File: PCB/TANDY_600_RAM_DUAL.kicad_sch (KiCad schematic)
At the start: 5 parts, among them J1 DIN 41612 2x22 male right-ang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, U1 628128_SOP, U2 74HC08

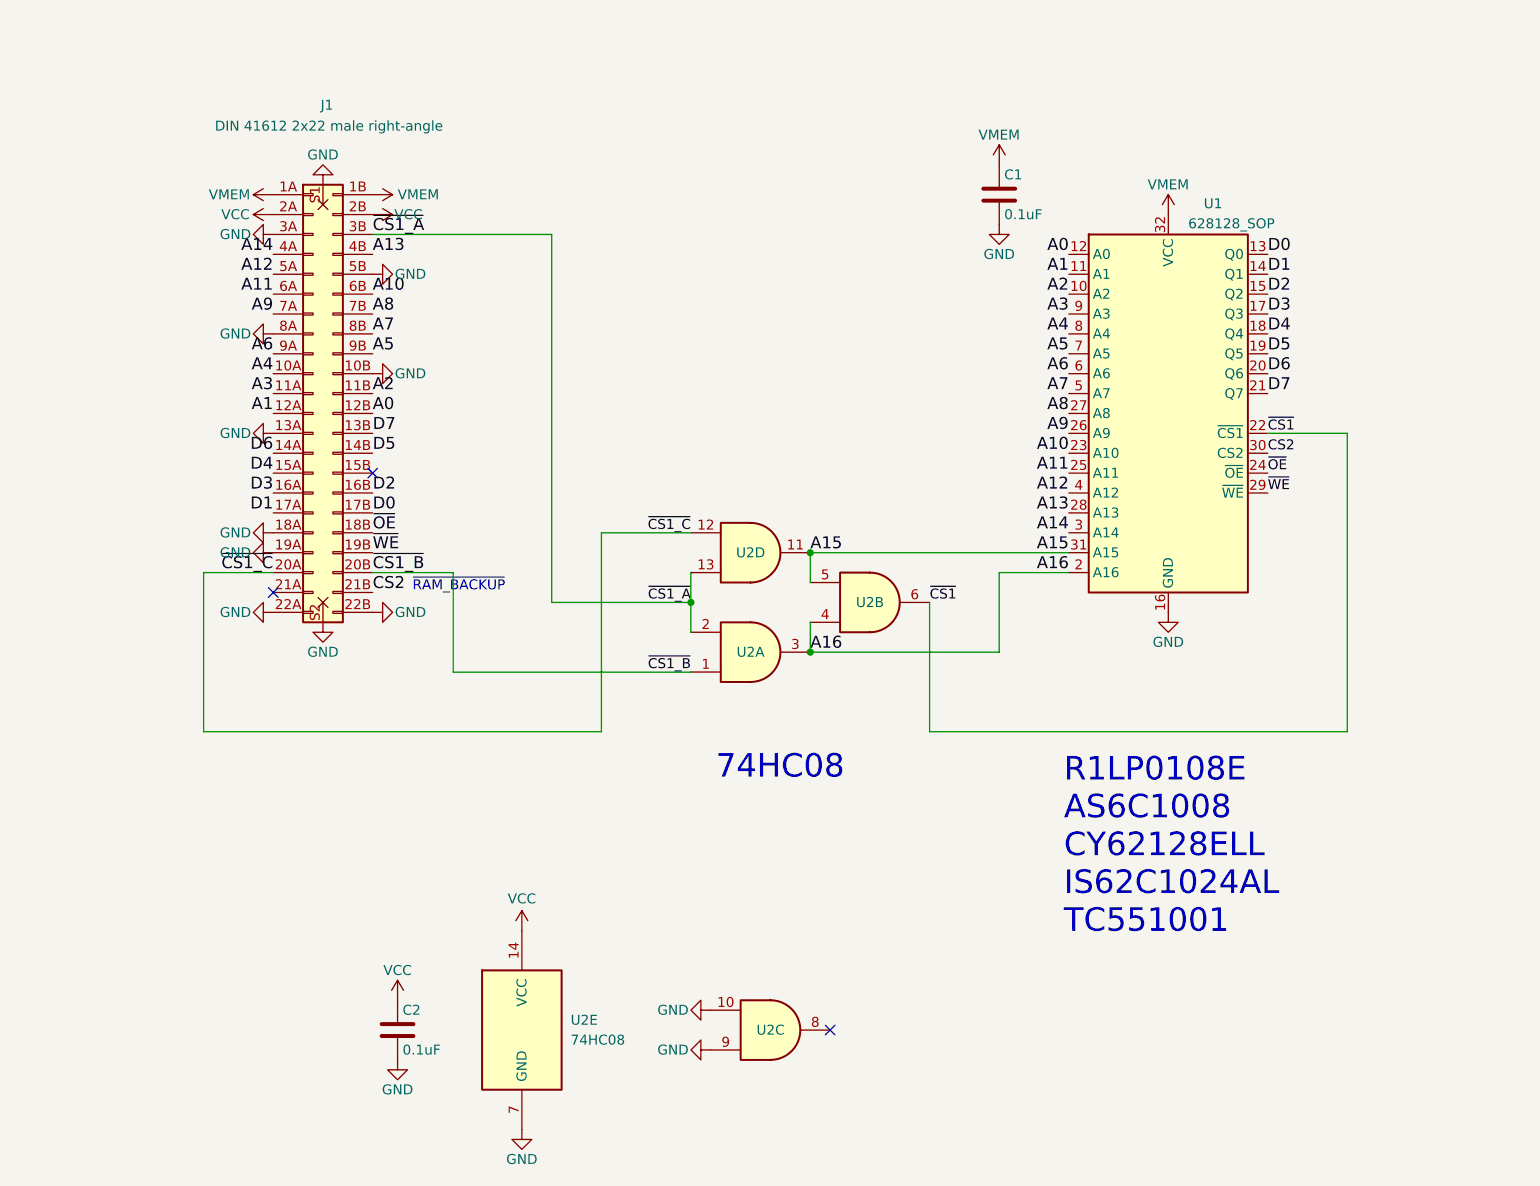
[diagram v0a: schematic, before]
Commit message: add DUAL version
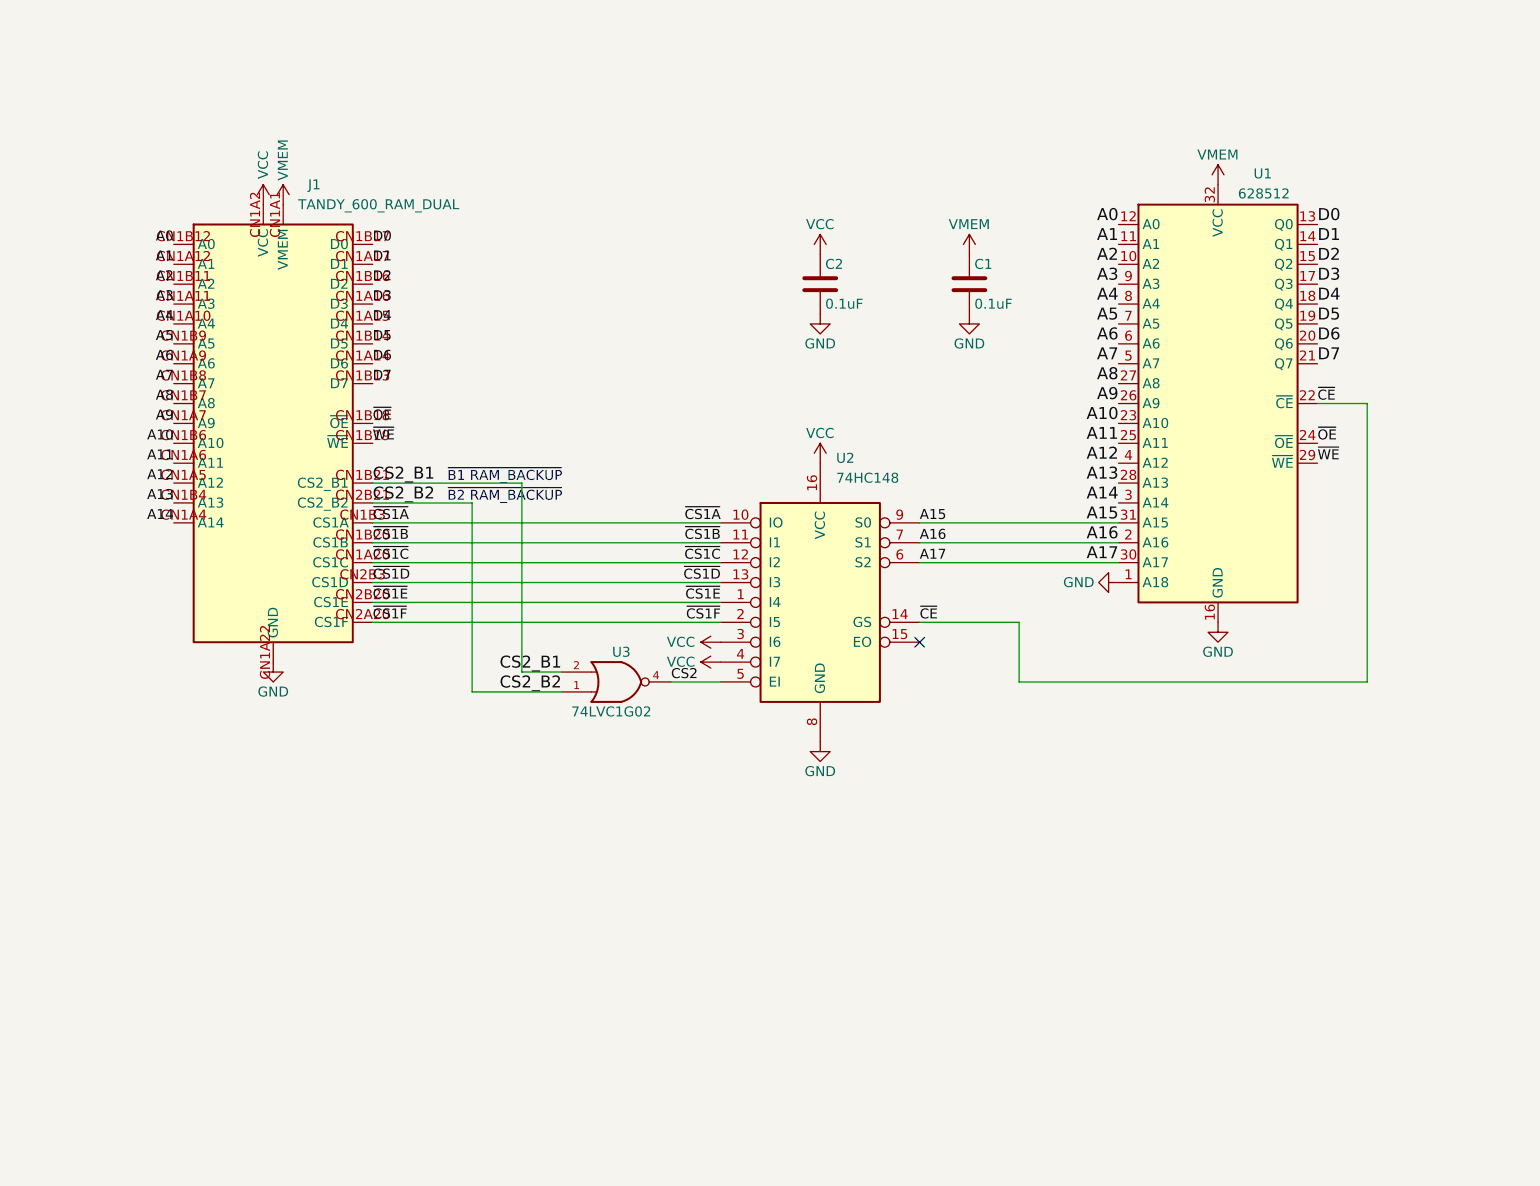
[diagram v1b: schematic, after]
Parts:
- removed J1: DIN 41612 2x22 male right-angle, 000_LOCAL:DIN 41612 2x22 male right-angle, symbol 000_LOCAL:DIN 41612 2x22 male right-angle
- removed U2: 74HC08, 000_LOCAL:SOIC-14_3.9x8.7mm_P1.27mm, symbol 000_LOCAL:74HC08
- added J1: TANDY_600_RAM_DUAL, 000_LOCAL:TANDY_600_RAM_DUAL, symbol 000_LOCAL:TANDY_600_RAM_DUAL
- added U2: 74HC148, 000_LOCAL:SOIC-16_4x10, symbol 000_LOCAL:74HC148
- added U3: 74LVC1G02, 000_LOCAL:SOT-353_SC-70-5, symbol 74xGxx:74LVC1G02
- C1, C2: footprint 000_LOCAL:C_1206 -> 000_LOCAL:C_0805
- U1: value 628128_SOP -> 628512; footprint 000_LOCAL:SOP-32W -> 000_LOCAL:TSOP32-14mm; symbol 000_LOCAL:628128_SOP -> 000_LOCAL:628512
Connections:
- net A0: now also J1.CN1B12 (A0), J1.CN2B12 (A0)
- net A1: now also J1.CN1A12 (A1), J1.CN2A12 (A1)
- net A10: now also J1.CN1B6 (A10), J1.CN2B6 (A10)
- net A11: now also J1.CN1A6 (A11), J1.CN2A6 (A11)
- net A12: now also J1.CN1A5 (A12), J1.CN2A5 (A12)
- net A13: now also J1.CN1B4 (A13), J1.CN2B4 (A13)
- net A14: now also J1.CN1A4 (A14), J1.CN2A4 (A14)
- net A15: now also U2.9 (S0)
- net A16: now also U2.7 (S1)
- net A2: now also J1.CN1B11 (A2), J1.CN2B11 (A2)
- net A3: now also J1.CN1A11 (A3), J1.CN2A11 (A3)
- net A4: now also J1.CN1A10 (A4), J1.CN2A10 (A4)
- net A5: now also J1.CN1B9 (A5), J1.CN2B9 (A5)
- net A6: now also J1.CN1A9 (A6), J1.CN2A9 (A6)
- net A7: now also J1.CN1B8 (A7), J1.CN2B8 (A7)
- net A8: now also J1.CN1B7 (A8), J1.CN2B7 (A8)
- net A9: now also J1.CN1A7 (A9), J1.CN2A7 (A9)
- net CS2: now also U2.5 (EI), U3.4; no longer U1.30 (CS2)
- net D0: now also J1.CN1B17 (D0), J1.CN2B17 (D0)
- net D1: now also J1.CN1A17 (D1), J1.CN2A17 (D1)
- net D2: now also J1.CN1B16 (D2), J1.CN2B16 (D2)
- net D3: now also J1.CN1A16 (D3), J1.CN2A16 (D3)
- net D4: now also J1.CN1A15 (D4), J1.CN2A15 (D4)
- net D5: now also J1.CN1B14 (D5), J1.CN2B14 (D5)
- net D6: now also J1.CN1A14 (D6), J1.CN2A14 (D6)
- net D7: now also J1.CN1B13 (D7), J1.CN2B13 (D7)
- net GND: now also U1.1 (A18), J1.CN1A13 (GND), J1.CN1A18 (GND), J1.CN1A19 (GND), J1.CN1A22 (GND), J1.CN1A3 (GND), J1.CN1A8 (GND), J1.CN1B10 (GND), J1.CN1B22 (GND), J1.CN1B5 (GND), J1.CN2A13 (GND), J1.CN2A18 (GND), J1.CN2A19 (GND), J1.CN2A22 (GND), J1.CN2A3 (GND), J1.CN2A8 (GND), J1.CN2B10 (GND), J1.CN2B22 (GND), J1.CN2B5 (GND), U2.8 (GND), U3.3 (GND)
- net VCC: now also J1.CN1A2 (VCC), J1.CN1B2 (VCC), J1.CN2A2 (VCC), J1.CN2B2 (VCC), U2.16 (VCC), U2.3 (I6), U2.4 (I7), U3.5 (VCC)
- net VMEM: now also J1.CN1A1 (VMEM), J1.CN1B1 (VMEM), J1.CN2A1 (VMEM), J1.CN2B1 (VMEM)
- net ~{OE}: now also J1.CN1B18 (~{OE}), J1.CN2B18 (~{OE})
- net ~{WE}: now also J1.CN1B19 (~{WE}), J1.CN2B19 (~{WE})
- net ~{CS1} renamed ~{CE}
- net ~{CE}: now also U2.14 (GS)
- new net A17: U1.30 (A17), U2.6 (S2)
- new net CS2_B1: J1.CN1B21 (CS2_B1), U3.2
- new net CS2_B2: J1.CN2B21 (CS2_B2), U3.1
- new net ~{CS1A}: J1.CN1B3 (CS1A), U2.10 (IO)
- new net ~{CS1B}: J1.CN1B20 (CS1B), U2.11 (I1)
- new net ~{CS1C}: J1.CN1A20 (CS1C), U2.12 (I2)
- new net ~{CS1D}: J1.CN2B3 (CS1D), U2.13 (I3)
- new net ~{CS1E}: J1.CN2B20 (CS1E), U2.1 (I4)
- new net ~{CS1F}: J1.CN2A20 (CS1F), U2.2 (I5)
- no-connect marks 3 -> 1
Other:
- note added: "~{B1 RAM_BACKUP}"
- note added: "~{B2 RAM_BACKUP}"
- note removed: "74HC08"
- note removed: "R1LP0108E AS6C1008 CY62128ELL IS62C1024AL TC551001"
- note removed: "~{RAM_BACKUP}"
- title: TANDY 600 RAM -> TANDY 600 DUAL RAM

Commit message: wrong sram pinout on dual version
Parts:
- U1: value 628512 -> AS6C4008_TSOP-I_sTSOP; footprint 000_LOCAL:TSOP32-14mm -> 000_LOCAL:TSOP32-dual; symbol 000_LOCAL:628512 -> 000_LOCAL:AS6C4008_TSOP-I_sTSOP
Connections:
- net A0: now also U1.20 (A0); no longer U1.12 (A0)
- net A1: now also U1.19 (A1); no longer U1.11 (A1)
- net A10: now also U1.31 (A10); no longer U1.23 (A10)
- net A11: now also U1.1 (A11); no longer U1.25 (A11)
- net A12: now also U1.12 (A12); no longer U1.4 (A12)
- net A13: now also U1.4 (A13); no longer U1.28 (A13)
- net A14: now also U1.11 (A14); no longer U1.3 (A14)
- net A15: now also U1.7 (A15); no longer U1.31 (A15)
- net A16: now also U1.10 (A16); no longer U1.2 (A16)
- net A17: now also U1.6 (A17); no longer U1.30 (A17)
- net A2: now also U1.18 (A2); no longer U1.10 (A2)
- net A3: now also U1.17 (A3); no longer U1.9 (A3)
- net A4: now also U1.16 (A4); no longer U1.8 (A4)
- net A5: now also U1.15 (A5); no longer U1.7 (A5)
- net A6: now also U1.14 (A6); no longer U1.6 (A6)
- net A7: now also U1.13 (A7); no longer U1.5 (A7)
- net A8: now also U1.3 (A8); no longer U1.27 (A8)
- net A9: now also U1.2 (A9); no longer U1.26 (A9)
- net D0: now also U1.21 (Q0); no longer U1.13 (Q0)
- net D1: now also U1.22 (Q1); no longer U1.14 (Q1)
- net D2: now also U1.23 (Q2); no longer U1.15 (Q2)
- net D3: now also U1.25 (Q3); no longer U1.17 (Q3)
- net D4: now also U1.26 (Q4); no longer U1.18 (Q4)
- net D5: now also U1.27 (Q5); no longer U1.19 (Q5)
- net D6: now also U1.28 (Q6); no longer U1.20 (Q6)
- net D7: now also U1.29 (Q7); no longer U1.21 (Q7)
- net GND: now also U1.24 (GND), U1.9 (A18); no longer U1.1 (A18), U1.16 (GND)
- net VMEM: now also U1.8 (VCC); no longer U1.32 (VCC)
- net ~{CE}: now also U1.30 (~{CE}); no longer U1.22 (~{CE})
- net ~{OE}: now also U1.32 (~{OE}); no longer U1.24 (~{OE})
- net ~{WE}: now also U1.5 (~{WE}); no longer U1.29 (~{WE})
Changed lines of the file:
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@@
   (title_block
     (title "TANDY 600 DUAL RAM")
-    (date "2022-09-29")
-    (rev "001")
+    (date "2022-09-30")
+    (rev "002")
     (company "Brian K. White - b.kenyon.w@gmail.com")
     (comment 1 "LICENSE: CC-BY-SA 4.0")
@@
     (pin "1")
   )
-  (symbol (lib_id "000_LOCAL:628512") (at 190.5 82.55 0) (unit 1)
+  (symbol (lib_id "000_LOCAL:AS6C4008_TSOP-I_sTSOP") (at 190.5 82.55 0) (unit 1)
     (in_bom yes) (on_board yes)
     (property "Reference" "U1" (id 0) (at 196.215 55.753 0))
-    (property "Value" "628512" (id 1) (at 193.04 59.055 0)
+    (property "Value" "AS6C4008_TSOP-I_sTSOP" (id 1) (at 193.04 59.055 0)
       (effects (font (size 1.27 1.27)) (justify left bottom))
     )
-    (property "Footprint" "000_LOCAL:TSOP32-14mm" (id 2) (at 190.5 82.55 0)
-      (effects (font (size 1.27 1.27)) hide)
-    )
-    (property "Datasheet" "http://www.futurlec.com/Datasheet/Memory/628512.pdf" (id 3) (at 190.5 82.55 0)
-      (effects (font (size 1.27 1.27)) hide)
-    )
-    (pin "16")
-    (pin "32")
+    (property "Footprint" "000_LOCAL:TSOP32-dual" (id 2) (at 190.5 82.55 0)
+      (effects (font (size 1.27 1.27)) hide)
+    )
+    (property "Datasheet" "https://www.alliancememory.com/wp-content/uploads/pdf/AS6C4008.pdf" (id 3) (at 190.5 82.55 0)
+      (effects (font (size 1.27 1.27)) hide)
+    )
+    (pin "24")
+    (pin "8")
     (pin "1")
     (pin "10")
@@
     (pin "14")
     (pin "15")
+    (pin "16")
     (pin "17")
     (pin "18")
@@
     (pin "22")
     (pin "23")
-    (pin "24")
     (pin "25")
     (pin "26")
@@
     (pin "30")
     (pin "31")
+    (pin "32")
     (pin "4")
     (pin "5")
     (pin "6")
     (pin "7")
-    (pin "8")
     (pin "9")
   )
@@
     )
     (path "/00000000-0000-0000-0000-0000613c8a04"
-      (reference "U1") (unit 1) (value "628512") (footprint "000_LOCAL:TSOP32-14mm")
+      (reference "U1") (unit 1) (value "AS6C4008_TSOP-I_sTSOP") (footprint "000_LOCAL:TSOP32-dual")
     )
     (path "/88b9c531-ca53-4b2a-bf55-7a2b00d5c199"
